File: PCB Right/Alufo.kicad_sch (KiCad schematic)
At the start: 31 parts, among them J2 USB_C_Receptacle_USB2.0_16P_2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, J4 USB_C_Receptacle_USB2.0_16P_2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, SW2 BOOT, U2 CH552T, U4 USBLC6-2P6, U6 USBLC6-2P6

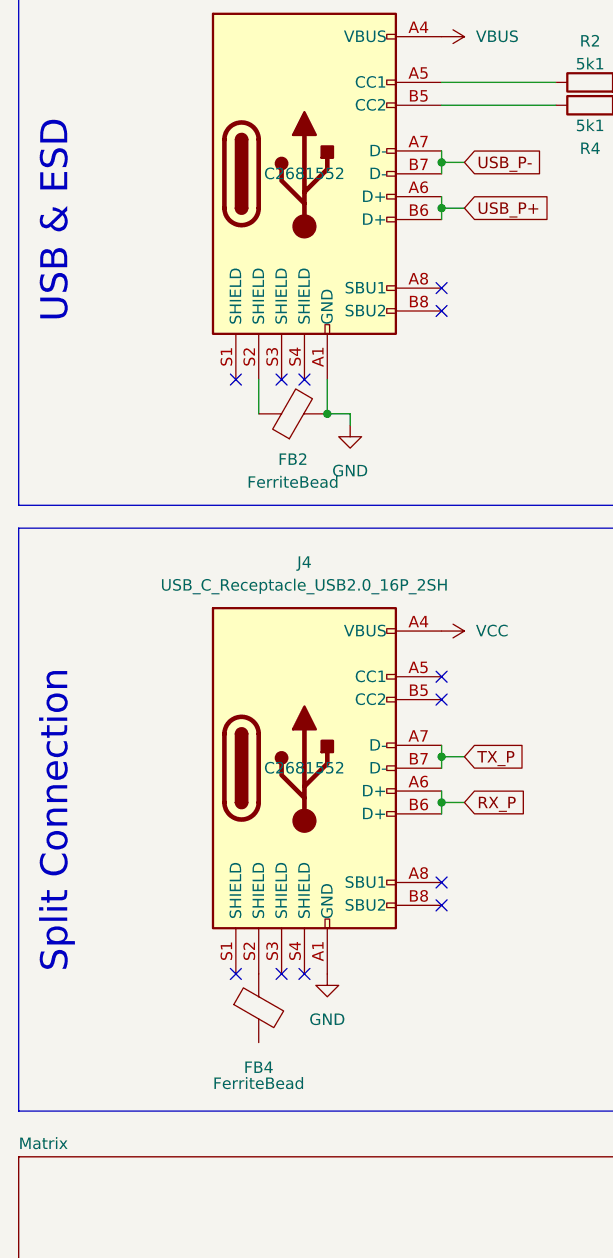
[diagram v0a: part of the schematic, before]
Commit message: Add shield connectors
The USB ports will now be connected to the aluminium PCB core. This is done using a 0.6mm diameter wire. One end of the wire will be soldered to a pad on the PCB and the other will pass through a hole to friction fit against the aluminium core.

Also, R9, the 0Ω resistor on the lefthand VCC line has returned to allow a more direct ground route between the USB port and the MCU. However it is now a smaller 0805 size resistor.
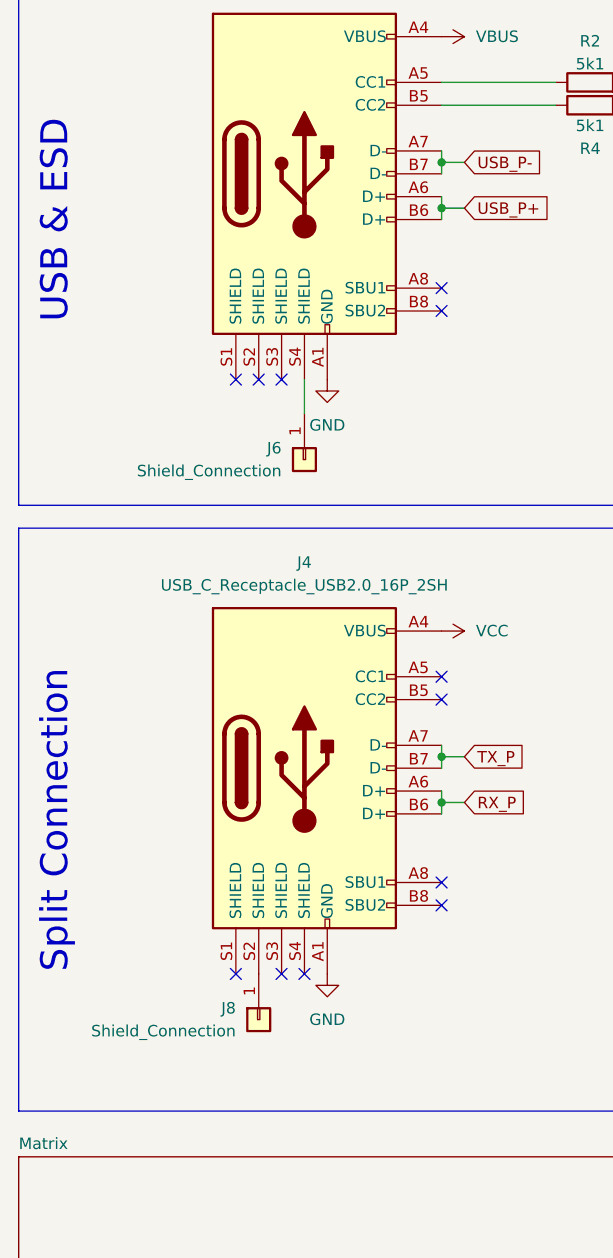
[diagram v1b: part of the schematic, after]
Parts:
- removed FB2, FB4: FerriteBead, Inductor_SMD:L_0805_2012Metric, symbol Device:FerriteBead
- added J6, J8: Shield_Connection, Project_Library:Shield_Connector, symbol Connector_Generic:Conn_01x01
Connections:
- net at J2.S4 (SHIELD): now also J6.1 (Pin_1)
- net at J4.S2 (SHIELD): now also J8.1 (Pin_1)
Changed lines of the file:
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@@
 	)
 	(junction
-		(at 49.53 127)
-		(diameter 0)
-		(color 0 0 0 0)
-	)
-	(junction
 		(at 74.93 45.72)
 		(diameter 0)
@@
 	)
 	(no_connect
-		(at 46.99 123.19)
+		(at 41.91 123.19)
 	)
 	(no_connect
@@
 	(wire
 		(pts
-			(xy 52.07 127) (xy 49.53 127)
-		)
-		(stroke
-			(width 0)
-			(type default)
-		)
-	)
-	(wire
-		(pts
 			(xy 118.11 91.44) (xy 123.19 91.44)
 		)
@@
 	(wire
 		(pts
-			(xy 41.91 123.19) (xy 41.91 127)
+			(xy 134.62 43.18) (xy 128.27 43.18)
 		)
 		(stroke
@@
 	(wire
 		(pts
-			(xy 134.62 43.18) (xy 128.27 43.18)
+			(xy 82.55 91.44) (xy 82.55 92.71)
 		)
 		(stroke
@@
 	(wire
 		(pts
-			(xy 82.55 91.44) (xy 82.55 92.71)
+			(xy 60.96 48.26) (xy 62.23 48.26)
 		)
 		(stroke
@@
 	(wire
 		(pts
-			(xy 60.96 48.26) (xy 62.23 48.26)
+			(xy 74.93 43.18) (xy 77.47 43.18)
 		)
 		(stroke
@@
 	(wire
 		(pts
-			(xy 74.93 43.18) (xy 77.47 43.18)
+			(xy 64.77 99.06) (xy 62.23 99.06)
 		)
 		(stroke
@@
 	(wire
 		(pts
-			(xy 64.77 99.06) (xy 62.23 99.06)
+			(xy 46.99 127) (xy 46.99 123.19)
 		)
 		(stroke
@@
 	(wire
 		(pts
-			(xy 52.07 127) (xy 52.07 128.27)
-		)
-		(stroke
-			(width 0)
-			(type default)
-		)
-	)
-	(wire
-		(pts
 			(xy 62.23 99.06) (xy 62.23 100.33)
 		)
@@
 	(wire
 		(pts
-			(xy 49.53 123.19) (xy 49.53 127)
-		)
-		(stroke
-			(width 0)
-			(type default)
-		)
-	)
-	(wire
-		(pts
 			(xy 134.62 91.44) (xy 135.128 91.44)
 		)
@@
 					(size 1.27 1.27)
 				)
+				(hide yes)
 			)
 		)
@@
 					(size 1.27 1.27)
 				)
+				(hide yes)
 			)
 		)
@@
 	)
 	(symbol
+		(lib_id "Connector_Generic:Conn_01x01")
+		(at 41.91 194.31 90)
+		(mirror x)
+		(unit 1)
+		(exclude_from_sim no)
+		(in_bom yes)
+		(on_board yes)
+		(dnp no)
+		(property "Reference" "J8"
+			(at 39.37 193.04 90)
+			(effects
+				(font
+					(size 1.27 1.27)
+				)
+				(justify left)
+			)
+		)
+		(property "Value" "Shield_Connection"
+			(at 39.37 195.58 90)
+			(effects
+				(font
+					(size 1.27 1.27)
+				)
+				(justify left)
+			)
+		)
+		(property "Footprint" "Project_Library:Shield_Connector"
+			(at 41.91 194.31 0)
+			(effects
+				(font
+					(size 1.27 1.27)
+				)
+				(hide yes)
+			)
+		)
+		(property "Datasheet" "~"
+			(at 41.91 194.31 0)
+			(effects
+				(font
+					(size 1.27 1.27)
+				)
+				(hide yes)
+			)
+		)
+		(property "Description" "Generic connector, single row, 01x01, script generated (kicad-library-utils/schlib/autogen/connector/)"
+			(at 41.91 194.31 0)
+			(effects
+				(font
+					(size 1.27 1.27)
+				)
+				(hide yes)
+			)
+		)
+		(pin "1"
+		)
+		(instances
+			(project "Alufo"
+				(path "/52f043ac-ccff-4c85-bc10-2db9d3c9e3f3"
+					(reference "J8")
+					(unit 1)
+				)
+			)
+		)
+	)
+	(symbol
 		(lib_id "Device:C")
 		(at 74.93 36.83 180)
@@
 	)
 	(symbol
-		(lib_id "Device:FerriteBead")
-		(at 45.72 127 90)
-		(unit 1)
-		(exclude_from_sim no)
-		(in_bom yes)
-		(on_board yes)
-		(dnp no)
-		(property "Reference" "FB2"
-			(at 45.72 132.08 90)
-			(effects
-				(font
-					(size 1.27 1.27)
-				)
-			)
-		)
-		(property "Value" "FerriteBead"
-			(at 45.72 134.62 90)
-			(effects
-				(font
-					(size 1.27 1.27)
-				)
-			)
-		)
-		(property "Footprint" "Inductor_SMD:L_0805_2012Metric"
-			(at 45.72 128.778 90)
-			(effects
-				(font
-					(size 1.27 1.27)
-				)
-				(hide yes)
-			)
-		)
-		(property "Datasheet" "~"
-			(at 45.72 127 0)
-			(effects
-				(font
-					(size 1.27 1.27)
-				)
-				(hide yes)
-			)
-		)
-		(property "Description" "Ferrite bead"
-			(at 45.72 127 0)
-			(effects
-				(font
-					(size 1.27 1.27)
-				)
-				(hide yes)
-			)
-		)
-		(property "LCSC" "C20416196"
-			(at 45.72 127 0)
-			(effects
-				(font
-					(size 1.27 1.27)
-				)
-				(hide yes)
-			)
-		)
-		(pin "1"
-		)
-		(pin "2"
-		)
-		(instances
-			(project "Alufo"
-				(path "/52f043ac-ccff-4c85-bc10-2db9d3c9e3f3"
-					(reference "FB2")
-					(unit 1)
-				)
-			)
-		)
-	)
-	(symbol
 		(lib_id "Device:C")
 		(at 74.93 52.07 0)
@@
 	(symbol
 		(lib_id "power:GND")
-		(at 52.07 128.27 0)
+		(at 49.53 123.19 0)
 		(unit 1)
 		(exclude_from_sim no)
@@
 		(fields_autoplaced yes)
 		(property "Reference" "#PWR025"
-			(at 52.07 134.62 0)
+			(at 49.53 129.54 0)
 			(effects
 				(font
@@
 		)
 		(property "Value" "GND"
-			(at 52.07 133.35 0)
+			(at 49.53 128.27 0)
 			(effects
 				(font
@@
 		)
 		(property "Footprint" ""
-			(at 52.07 128.27 0)
+			(at 49.53 123.19 0)
 			(effects
 				(font
@@
 		)
 		(property "Datasheet" ""
-			(at 52.07 128.27 0)
+			(at 49.53 123.19 0)
 			(effects
 				(font
@@
 		)
 		(property "Description" "Power symbol creates a global label with name \"GND\" , ground"
-			(at 52.07 128.27 0)
+			(at 49.53 123.19 0)
 			(effects
 				(font
@@
 	)
 	(symbol
-		(lib_id "Device:FerriteBead")
-		(at 41.91 193.04 0)
+		(lib_id "Connector_Generic:Conn_01x01")
+		(at 46.99 132.08 90)
+		(mirror x)
 		(unit 1)
 		(exclude_from_sim no)
@@
 		(on_board yes)
 		(dnp no)
-		(property "Reference" "FB4"
-			(at 41.91 199.644 0)
+		(property "Reference" "J6"
+			(at 44.45 130.81 90)
 			(effects
 				(font
 					(size 1.27 1.27)
 				)
+				(justify left)
 			)
 		)
-		(property "Value" "FerriteBead"
-			(at 41.91 201.422 0)
+		(property "Value" "Shield_Connection"
+			(at 44.45 133.35 90)
 			(effects
 				(font
 					(size 1.27 1.27)
 				)
+				(justify left)
 			)
 		)
-		(property "Footprint" "Inductor_SMD:L_0805_2012Metric"
-			(at 40.132 193.04 90)
+		(property "Footprint" "Project_Library:Shield_Connector"
+			(at 46.99 132.08 0)
 			(effects
 				(font
@@
 		)
 		(property "Datasheet" "~"
-			(at 41.91 193.04 0)
-			(effects
-				(font
-					(size 1.27 1.27)
-				)
-				(hide yes)
-			)
-		)
-		(property "Description" "Ferrite bead"
-			(at 41.91 193.04 0)
+			(at 46.99 132.08 0)
 			(effects
 				(font
@@
 			)
 		)
-		(property "LCSC" "C20416196"
-			(at 41.91 193.04 0)
+		(property "Description" "Generic connector, single row, 01x01, script generated (kicad-library-utils/schlib/autogen/connector/)"
+			(at 46.99 132.08 0)
 			(effects
 				(font
@@
 		(pin "1"
 		)
-		(pin "2"
-		)
 		(instances
 			(project "Alufo"
 				(path "/52f043ac-ccff-4c85-bc10-2db9d3c9e3f3"
-					(reference "FB4")
+					(reference "J6")
 					(unit 1)
 				)

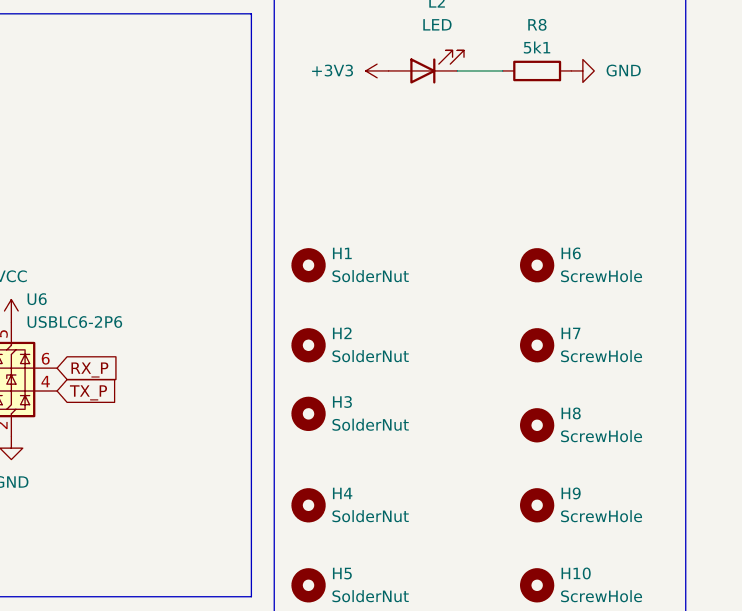
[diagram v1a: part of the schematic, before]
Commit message: Add shield connection to H3 (lower middle mounting hole)
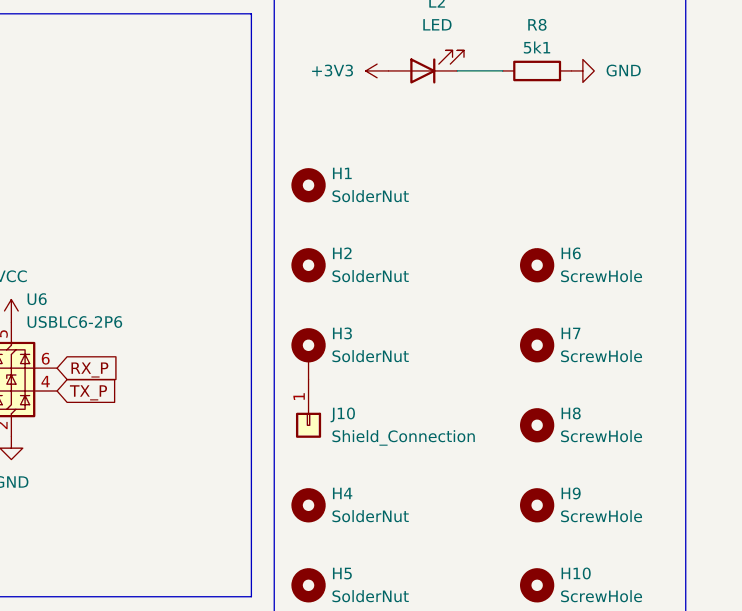
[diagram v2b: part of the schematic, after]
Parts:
- added J10: Shield_Connection, Project_Library:Shield_Connector, symbol Connector_Generic:Conn_01x01
- H3: footprint Project_Library:MountingHole_2.2mm_M2_SMD_Solder_Nut -> Project_Library:MountingHole_2.2mm_M2_SMD_Solder_Nut_Pad; symbol Mechanical:MountingHole -> Mechanical:MountingHole_Pad
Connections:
- new net: H3.1, J10.1 (Pin_1)
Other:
- moved on the sheet: H1, H2
